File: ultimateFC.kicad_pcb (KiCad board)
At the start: 8 copper layers, 30.4 x 25.2 mm, 190 parts, among them J1 USB_B_Micro, J2 10132797-011100LF, J3 10132797-011100LF, J4 10132797-011100LF, J5 10132797-011100LF, J6 10132797-011100LF, Q1 DMP2066LSN-7, U1 EFM8BB21F16G-C-QFN20R, U10 NCP81253MNTBG, U11 SiZ200DT, U12 NCP81253MNTBG, U13 SiZ200DT, U14 TPS62824ADMQ, U15 SiZ200DT, U16 NCP81253MNTBG, U17 NCP81253MNTBG, U18 NCP81253MNTBG, U19 NCP81253MNTBG, U2 EFM8BB21F16G-C-QFN20R, U20 SiZ200DT, U21 SiZ200DT, U22 SiZ200DT, U23 SiZ200DT, U24 EFM8BB21F16G-C-QFN20R, U25 NCP81253MNTBG, U26 SiZ200DT, U27 NCP81253MNTBG, U28 NCP81253MNTBG, U29 SiZ200DT, U3 NCP81253MNTBG, U30 SiZ200DT, U31 INA186, U33 STM32F745VGHx, U34 AB7456, U35 ZOE-M8Q_ZOE-M8Q, U36 ICM-20602, U37 S25FL064L, U39 BMP280, U4 SiZ200DT, U5 TPS630701, U6 EFM8BB21F16G-C-QFN20R, U7 NCP81253MNTBG, U8 SiZ200DT, U9 NCP81253MNTBG, X1 Molex_734120110, Y1 CSTNE8M00G550000R0, Y2 ECS-270-8-47Q-CES-TR

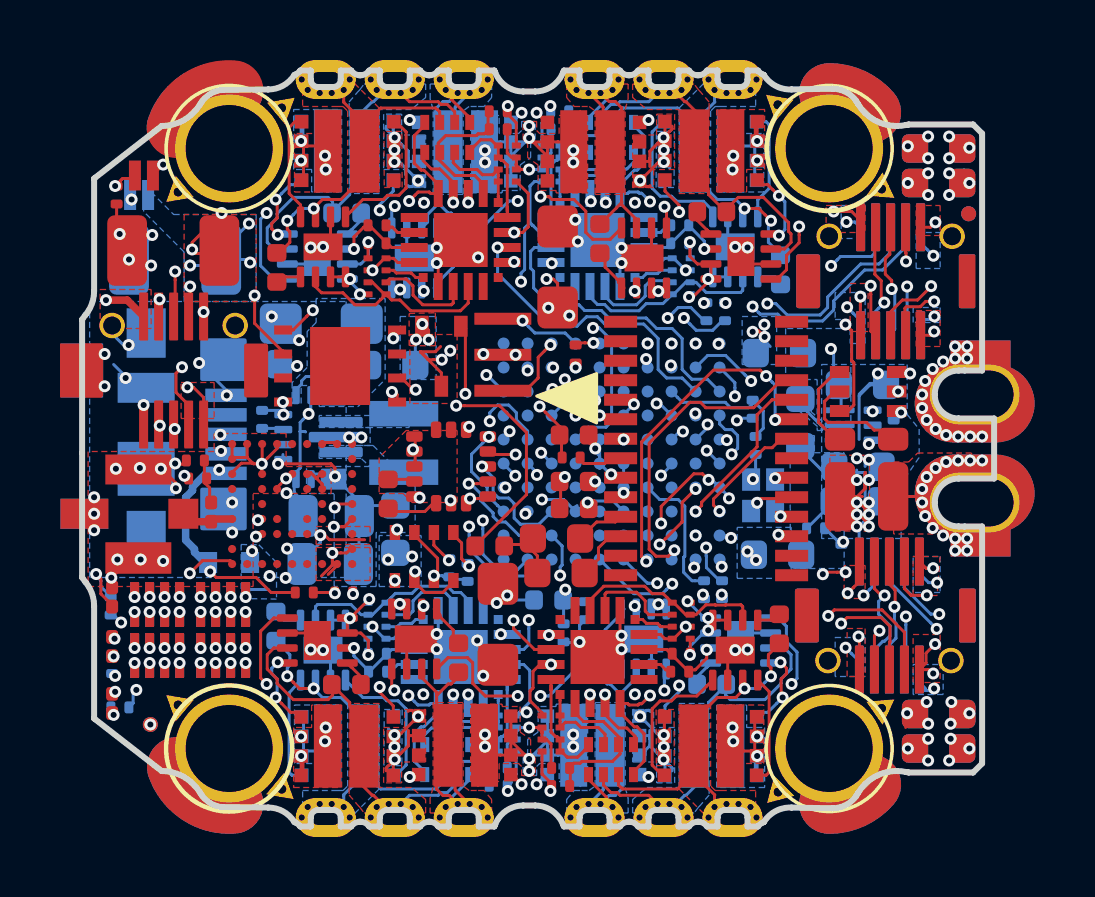
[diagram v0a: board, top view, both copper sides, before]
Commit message: update pcb to KiCad6 add assembly output gerbers
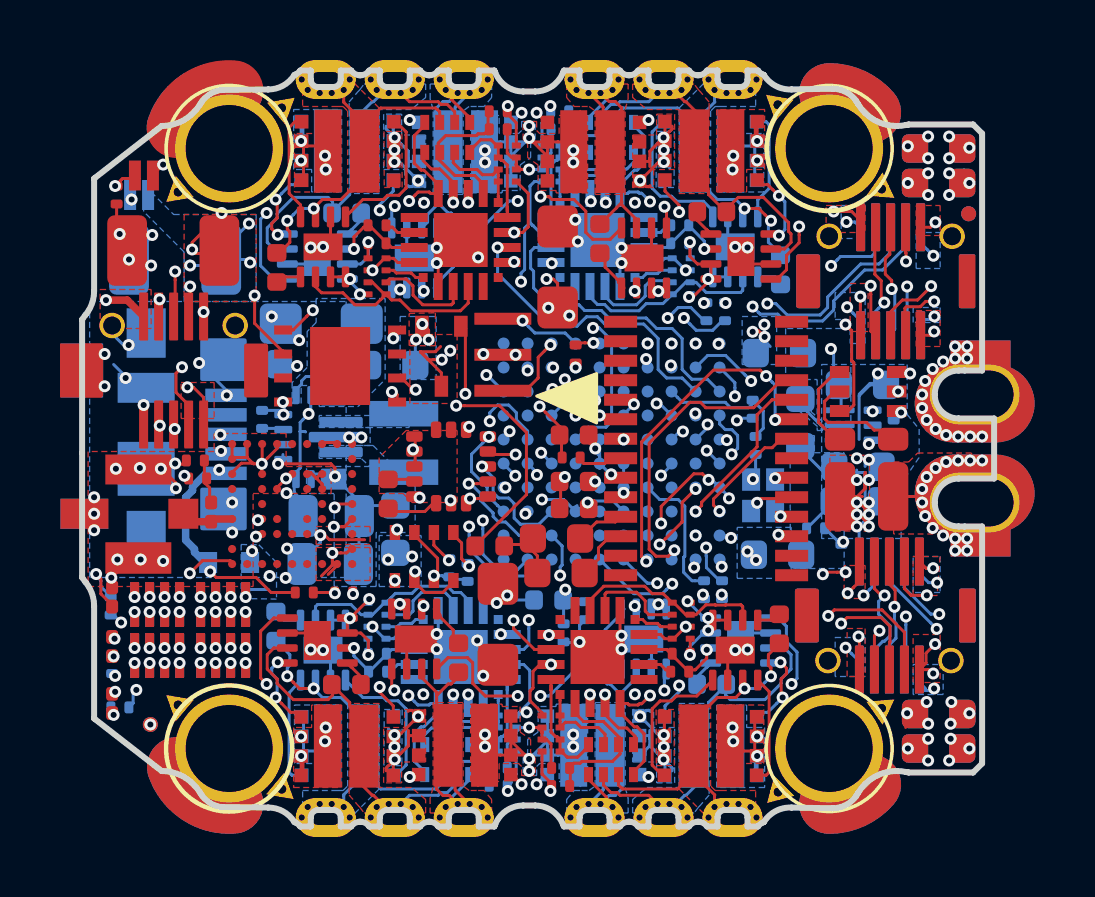
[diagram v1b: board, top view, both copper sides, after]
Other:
- net class Default removed
